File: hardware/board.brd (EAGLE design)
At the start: 53 x 30 mm, 46 parts, among them IC1 0915BM15A0001, J1 U.FL, U3 BLE113-A, X1 24MHz 8pF 10ppm -20C +70C, X3 MINI-USB-UX60-MB-5ST

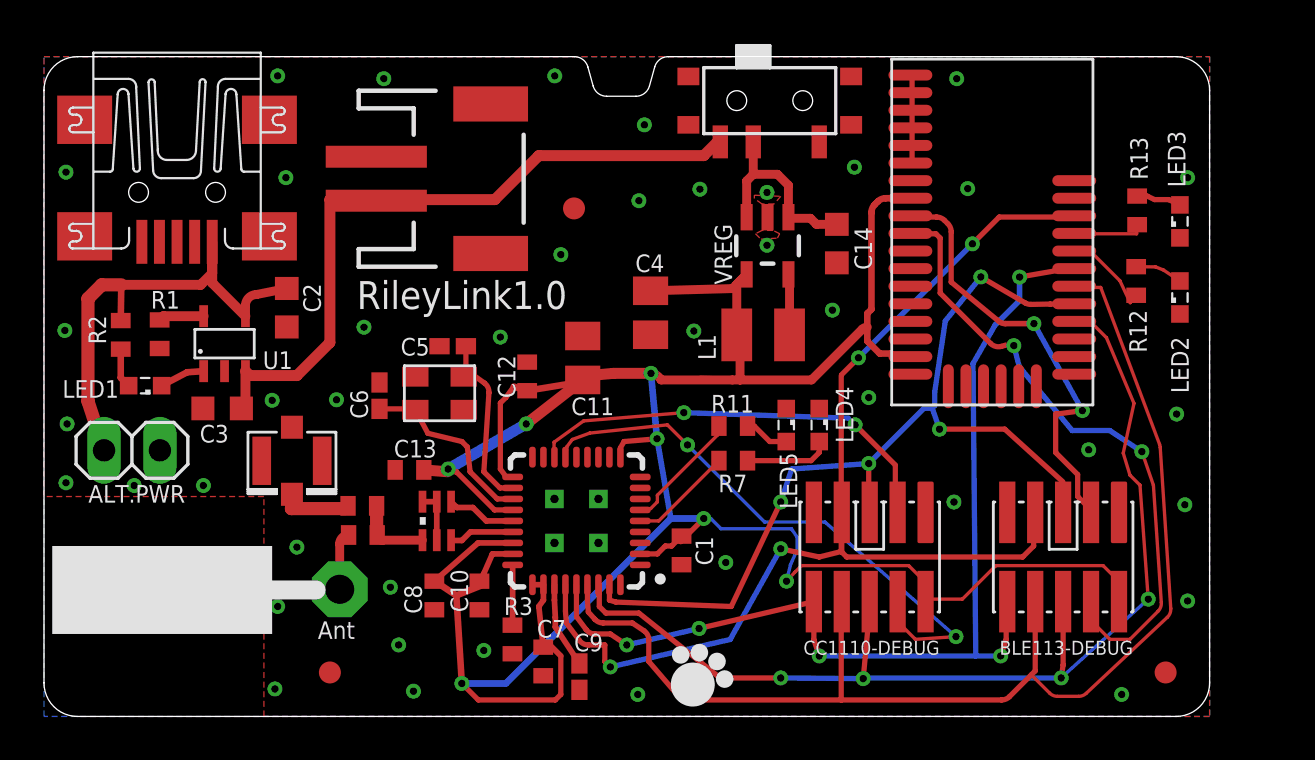
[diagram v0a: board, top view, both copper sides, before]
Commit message: JDBP changes: BOM adjustments, microUSB
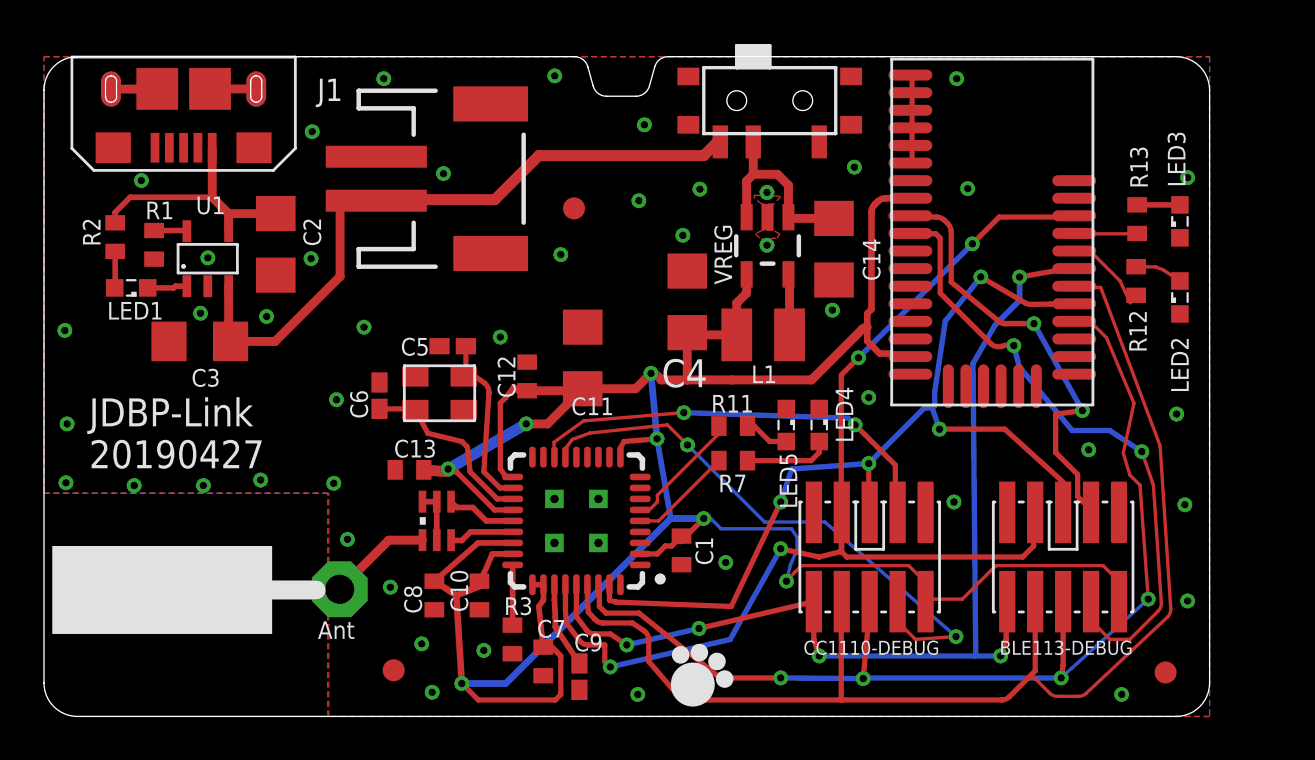
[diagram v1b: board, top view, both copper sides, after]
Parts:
- removed ALT.PWR: (no value), pinhead:1X02
- removed R4, R9: (no value), rcl:R0402
- removed X3: MINI-USB-UX60-MB-5ST, con-hirose:UX60-MB-5ST
- BLE113-DEBUG, CC1110-DEBUG: value CC-DEBUG-PWR -> 20021121-00010C4LF
- C11: device rcl:C0805K -> rcl:C1206
- C14, C2, C3: value 4.7uF -> 10uF; device rcl:C0603K -> rcl:C1206
- C4: value 10 uF -> 10uF; device rcl:C0805K -> rcl:C1206
- CC1110: value CC1110 -> CC1110F32RHHR
- IC1: value 0915BM15A0001 -> 0915BM15A0001E
- J1: value U.FL -> MF-CON-MICROUSB-RIGHT; device SparkFun-Connectors:U.FL -> MF_Connectors:MICROUSB-RIGHT
- JP1: value M02-JST-2MM-SMT -> S2B-PH-SM4-TB(LF)(SN)
- LED2, LED5: value blue -> red
- R11, R12, R13, R7: value 470 ohms -> 470
- R2: value 330 -> 470
- U1: value (none) -> MCP73831T
- U3: value BLE113-A -> BLE113-A-M256K
- VREG: value LM3671 -> LM3671MF-3.3/NOPB
- moved J1 16.3 mm to (6.35, 27.1), turned to 180 degrees
- moved LED1 4.49 mm to (3.96, 19.5)
- moved R2 4.45 mm to (3.24, 21.8)
- moved R1 4.07 mm to (5.01, 21.4)
- moved U1 3.94 mm to (6.10, 20.2)
- moved C3 3.21 mm to (7.08, 17.1)
- moved C2 2.92 mm to (10.5, 21.5)
- moved FID1 2.90 mm to (15.9, 2.10)
- moved C4 1.74 mm to (29.2, 18.9), turned to 90 degrees
- moved R13 0.40 mm to (49.7, 22.6)
- moved C14 0.28 mm to (35.9, 21.2)
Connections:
- removed net N$12: ANT1.1, R9.2
- removed net N$9: J1.P$3, R4.1
- net GND: now also J1.5, J1.S1, J1.S2, J1.S3, J1.S4, J1.S5, J1.S6; no longer ALT.PWR.1, J1.P$1, J1.P$2, X3.5
- net N$10: now also ANT1.1; no longer R4.2, R9.1
- net VIN_USB: now also J1.1; no longer ALT.PWR.2, X3.1
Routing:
- net VIN_USB: track 22.8 -> 11.4 mm
- net GND: track 7.00 -> 11.2 mm, vias 42 -> 45
- net N$9: track 3.29 -> 0.00 mm
- net N$12: track 2.64 -> 0.00 mm
- net N$10: track 3.57 -> 4.77 mm
- net VBAT: track 31.7 -> 30.6 mm
- net VDD: track 131.9 -> 131.2 mm
- net N$3: track 2.07 -> 1.52 mm
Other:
- board text added: "JDBP-Link 20190427"
- board text removed: "RileyLink1.0"

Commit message: More trace and part packing; DRC approvals
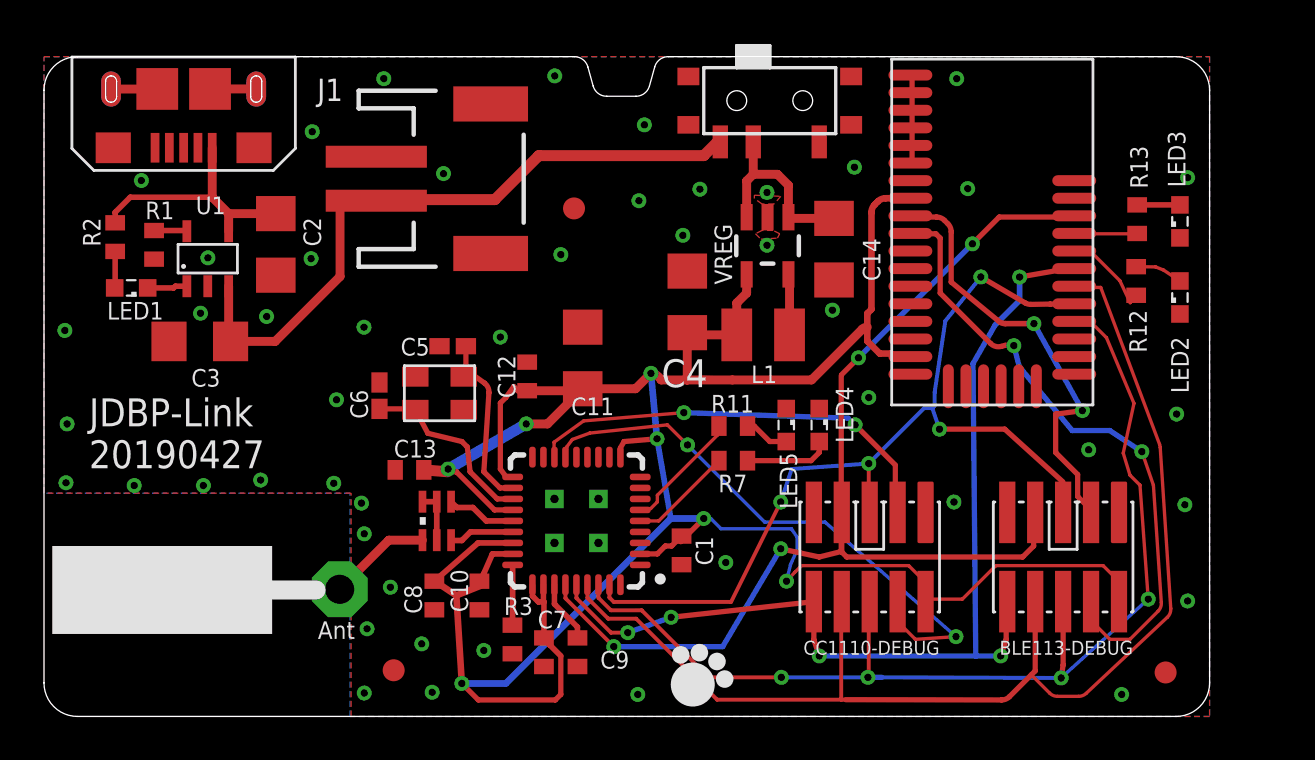
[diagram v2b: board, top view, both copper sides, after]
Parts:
- C9: device rcl:C0402K -> rcl:C0402
- moved C9 1.11 mm to (24.3, 2.92)
- moved C7 0.42 mm to (22.7, 2.92)
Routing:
- net RESET: track 52.8 -> 51.3 mm
- net N$18: track 3.91 -> 2.85 mm
- net MOSI: track 56.7 -> 55.7 mm
- net MISO: track 46.8 -> 46.0 mm
- net GND: vias 45 -> 48

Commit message: More changes
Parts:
- removed BLE113-DEBUG, CC1110-DEBUG: 20021121-00010C4LF, parts:CC-P05
- removed C13: 0.1uF, rcl:C0402
- removed C14: 10uF, rcl:C1206
- removed LED4: green, led:SML0603
- removed LED5: red, led:SML0603
- removed R11, R12, R13, R7: 470, rcl:R0402
- added C15: 0.1uF, rcl:C0402
- added C20: (no value), rcl:C0402
- added L2: (no value), rcl:R0402
- added R4, R5: 470, rcl:R0402
- added TC1, TC2: TC2050-IDC-NL, TagConnect:TC2050-IDC-NL
- ANT1: device discrete:PAD-01 -> board:0433AT62A0020
- C1: value 0.1uF -> 10uF; device rcl:C0402 -> rcl:C1206
- C11: value 10uF -> 0.1uF; device rcl:C1206 -> rcl:C0402
- C7: value 0.1uF -> 1uF
- C9: value 1uF -> 0.1uF
- IC1: value 0915BM15A0001E -> 0433BM15A0001
- R2: value 470 -> 56kOhm ± 1%
- R3: value 56kOhm ± 1% -> 470
- moved R2 38.3 mm to (37.2, 4.19), turned to 90 degrees
- moved R3 26.0 mm to (3.24, 22.2), turned to 270 degrees
- moved FID1 17.6 mm to (33.5, 1.78)
- moved C7 17.4 mm to (40.1, 2.92), turned to 90 degrees
- moved C6 16.4 mm to (31.6, 13.7)
- moved C8 16.3 mm to (34.0, 5.46)
- moved C5 16.0 mm to (34.6, 15.9)
- moved X1 16.0 mm to (34.0, 13.8)
- moved C10 16.0 mm to (35.8, 5.46)
- moved CC1110 15.9 mm to (40.1, 8.89)
- moved IC1 15.8 mm to (33.7, 8.64)
- moved C1 15.4 mm to (26.5, 22.7)
- moved JP1 14.4 mm to (4.64, 22.1), flipped to the bottom, turned to 0 degrees
- moved C9 14.4 mm to (38.6, 2.92), turned to 270 degrees
- moved C11 13.0 mm to (37.2, 13.6)
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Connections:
- removed net N$24: LED4.A, R7.1
- removed net N$25: LED5.A, R11.1
- new net N$1: ANT1.P$1, L2.2
- net DC: now also TC1.5; no longer CC1110-DEBUG.3
- net DC_BLE: now also TC2.5; no longer BLE113-DEBUG.3
- net DD: now also TC1.7; no longer CC1110-DEBUG.4
- net DD_BLE: now also TC2.7; no longer BLE113-DEBUG.4
- net GND: now also C15.2, C20.2, C7.1, C9.2, R2.1, TC1.1, TC2.1; no longer BLE113-DEBUG.1, C13.2, C14.2, C7.2, C9.1, CC1110-DEBUG.1, LED4.C, LED5.C, R3.1
- net MISO: now also TC1.2; no longer BLE113-DEBUG.10, CC1110-DEBUG.10
- net MOSI: now also TC1.6; no longer BLE113-DEBUG.8, CC1110-DEBUG.8
- net N$10: now also C20.1, L2.1; no longer ANT1.1
- net N$14: now also R2.2; no longer R3.2
- net N$18: now also C7.2; no longer C9.2
- net N$29: now also R4.1; no longer R12.1
- net N$30: now also R5.1; no longer R13.1
- net N$31: now also R4.2; no longer R12.2
- net N$32: now also R5.2; no longer R13.2
- net N$4: now also R3.2; no longer R2.2
- net P0_0: no longer R7.2
- net P0_1: no longer R11.2
- net RESET: now also TC1.8, TC2.8; no longer BLE113-DEBUG.7, CC1110-DEBUG.7
- net SCK: now also TC1.10; no longer BLE113-DEBUG.6, CC1110-DEBUG.6
- net SSN: now also TC1.9; no longer BLE113-DEBUG.5, CC1110-DEBUG.5
- net V+: now also C1.1; no longer C14.1
- net VDD: now also C15.1, C9.1, TC1.3, TC2.3; no longer BLE113-DEBUG.2, C1.1, C13.1, C7.1, CC1110-DEBUG.2
- net VIN_USB: now also R3.1; no longer R2.1
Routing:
- net VDD: track 131.5 -> 99.2 mm, vias 7 -> 8
- net MOSI: track 55.7 -> 31.0 mm, vias 0 -> 3
- net VBAT: track 30.6 -> 48.6 mm, vias 0 -> 1
- net SCK: track 49.7 -> 32.5 mm, vias 4 -> 3
- net SSN: track 44.3 -> 27.3 mm
- net MISO: track 46.0 -> 32.7 mm, vias 5 -> 3
- net DD: track 26.1 -> 13.9 mm, vias 2 -> 0
- net RESET: track 51.3 -> 39.9 mm, vias 4 -> 5
- net V+: track 8.93 -> 15.7 mm, vias 0 -> 2
- net DD_BLE: track 28.7 -> 22.5 mm
- net P0_1: track 5.55 -> 0.00 mm
- net DC: track 19.7 -> 14.3 mm, vias 2 -> 0
- net P0_0: track 4.71 -> 0.00 mm
- net N$24: track 3.91 -> 0.00 mm
- net GND: track 11.2 -> 8.39 mm, vias 48 -> 72
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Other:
- board size 53 x 30 mm -> 55.8 x 30 mm
- board text added: "PatchLink Jacob Berg Potter"
- board text removed: "JDBP-Link 20190427"
